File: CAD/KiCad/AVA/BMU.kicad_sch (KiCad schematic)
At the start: 9 parts, among them Q1 IRF9540N

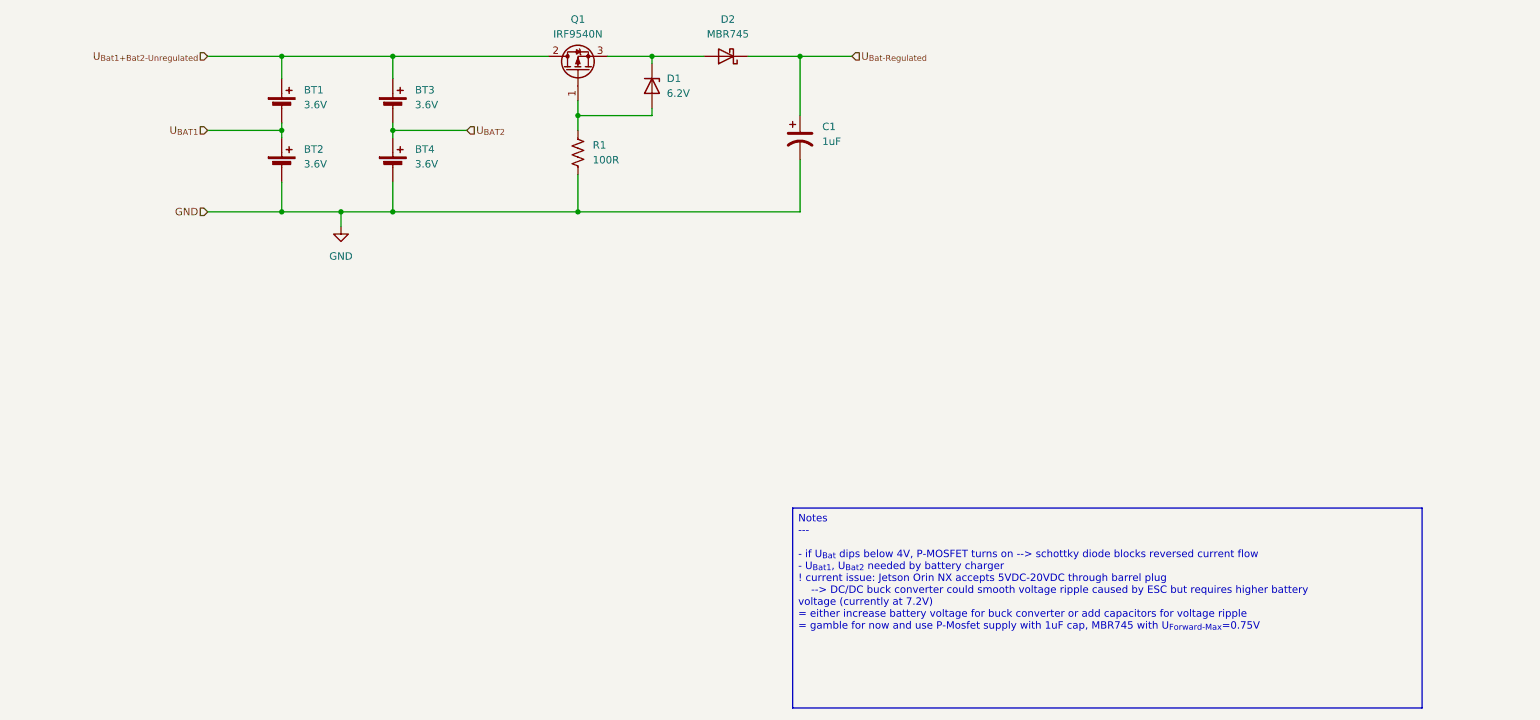
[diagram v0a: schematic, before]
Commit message: Added Graphos MBSE json file necessary for model
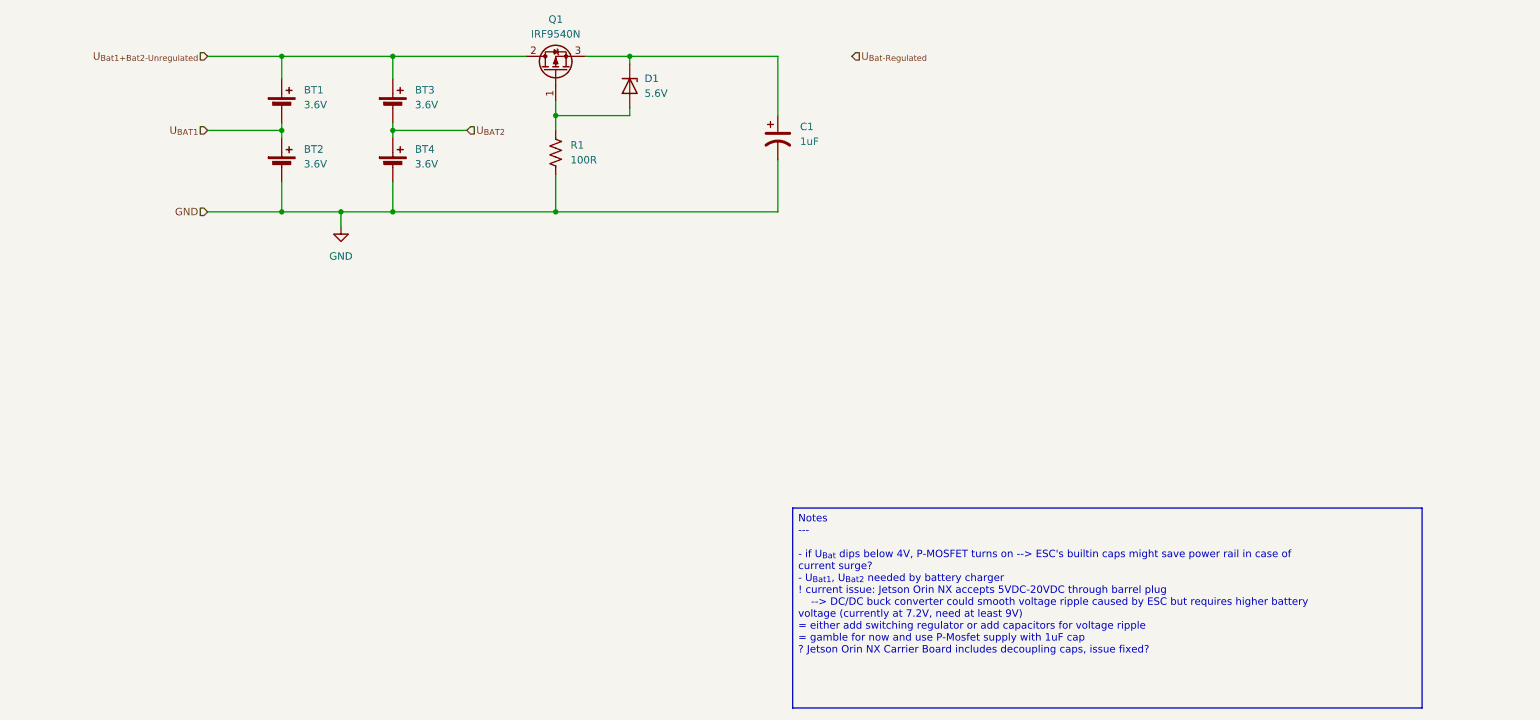
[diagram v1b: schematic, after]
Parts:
- removed D2: MBR745, Package_TO_SOT_THT:TO-220-2_Vertical, symbol Diode:MBR745
- D1: value 6.2V -> 5.6V
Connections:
- net U_{Bat-Regulated}: no longer C1.1
- net at D1.1 (K), Q1.3 (S): now also C1.1
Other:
- moved on the sheet: C1, D1, Q1, R1
